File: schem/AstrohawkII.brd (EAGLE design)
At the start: 100 x 80 mm, 4 parts, among them J1 RASPBERRYPI-40-PIN-GPIO_PTH_N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

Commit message: updates eagle schematic and board
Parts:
- removed J3: (no value), SparkFun-Connectors:1X04
- removed J4: (no value), SparkFun-Connectors:1X06
- added U$1: BNO055, rocketry:BNO055
- moved J1 28.1 mm to (58.0, 10.0), turned to 180 degrees
- moved J2 16.7 mm to (41.4, 26.1)
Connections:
- removed net 3VO: J2.3, J4.2
- removed net ADR: J3.4
- removed net PS0: J3.1
- removed net PS1: J3.2
- net GND: no longer J4.3
- net INT: now also J1.29; no longer J3.3
- net INT1: now also J1.32
- net INT2: now also J1.33
- net RST: now also J1.31; no longer J4.6
- net SCL: no longer J4.5
- net SDA: no longer J4.4
- net VIN: no longer J4.1
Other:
- board size 100 x 80 mm -> 64 x 56 mm
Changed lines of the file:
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@@
 <setting verticaltext="up"/>
 </settings>
-<grid distance="50" unitdist="mil" unit="mil" style="lines" multiple="1" display="no" altdistance="5" altunitdist="mil" altunit="mil"/>
+<grid distance="1" unitdist="mm" unit="mm" style="lines" multiple="1" display="no" altdistance="0.5" altunitdist="mm" altunit="mm"/>
 <layers>
 <layer number="1" name="Top" color="4" fill="1" visible="yes" active="yes"/>
@@
 <board>
 <plain>
-<wire x1="0" y1="0" x2="100" y2="0" width="0" layer="20"/>
-<wire x1="100" y1="0" x2="100" y2="80" width="0" layer="20"/>
-<wire x1="100" y1="80" x2="0" y2="80" width="0" layer="20"/>
-<wire x1="0" y1="80" x2="0" y2="0" width="0" layer="20"/>
+<wire x1="0" y1="0" x2="64" y2="0" width="0" layer="20"/>
+<wire x1="64" y1="0" x2="64" y2="56" width="0" layer="20"/>
+<wire x1="64" y1="56" x2="0" y2="56" width="0" layer="20"/>
+<wire x1="0" y1="56" x2="0" y2="0" width="0" layer="20"/>
+<dimension x1="3" y1="53" x2="61" y2="53" x3="32" y3="53" textsize="1.778" layer="1"/>
 </plain>
 <attributes>
@@
 </autorouter>
 <elements>
-<element name="J1" library="SparkFun-Connectors" package="2X20" value="RASPBERRYPI-40-PIN-GPIO_PTH_NO_SHROUD" x="33.02" y="22.86" smashed="yes">
-<attribute name="NAME" x="31.75" y="26.924" size="0.6096" layer="25" font="vector" ratio="20"/>
-<attribute name="VALUE" x="31.75" y="20.447" size="0.6096" layer="27" font="vector" ratio="20"/>
+<element name="J1" library="SparkFun-Connectors" package="2X20" value="RASPBERRYPI-40-PIN-GPIO_PTH_NO_SHROUD" x="58" y="10" smashed="yes" rot="R180">
+<attribute name="NAME" x="59.27" y="5.936" size="0.6096" layer="25" font="vector" ratio="20" rot="R180"/>
+<attribute name="VALUE" x="59.27" y="12.413" size="0.6096" layer="27" font="vector" ratio="20" rot="R180"/>
 </element>
-<element name="J2" library="SparkFun-Connectors" package="1X07" value="" x="33.02" y="40.64" smashed="yes">
-<attribute name="MPL3115A2" value="" x="63.5" y="30.48" size="1.778" layer="27" display="off"/>
-<attribute name="NAME" x="31.75" y="42.037" size="0.6096" layer="25" font="vector" ratio="20"/>
-<attribute name="VALUE" x="31.75" y="38.608" size="0.6096" layer="27" font="vector" ratio="20"/>
+<element name="J2" library="SparkFun-Connectors" package="1X07" value="" x="41.42" y="26.15" smashed="yes">
+<attribute name="MPL3115A2" value="" x="71.9" y="15.99" size="1.778" layer="27" display="off"/>
+<attribute name="NAME" x="41.15" y="28.547" size="0.6096" layer="25" font="vector" ratio="20"/>
+<attribute name="VALUE" x="40.15" y="24.118" size="0.6096" layer="27" font="vector" ratio="20"/>
 </element>
-<element name="J3" library="SparkFun-Connectors" package="1X04" value="" x="60.96" y="52.07" smashed="yes">
-<attribute name="BNO055X04" value="" x="83.82" y="34.29" size="1.778" layer="27" display="off"/>
-<attribute name="NAME" x="59.69" y="53.467" size="0.6096" layer="25" font="vector" ratio="20"/>
-<attribute name="PROD_ID" value="CONN-09696" x="83.82" y="34.29" size="1.778" layer="27" display="off"/>
-<attribute name="VALUE" x="59.69" y="50.038" size="0.6096" layer="27" font="vector" ratio="20"/>
-</element>
-<element name="J4" library="SparkFun-Connectors" package="1X06" value="" x="45.72" y="59.69" smashed="yes">
-<attribute name="BNO055X06" value="" x="73.66" y="45.72" size="1.778" layer="27" display="off"/>
-<attribute name="NAME" x="44.45" y="61.087" size="0.6096" layer="25" font="vector" ratio="20"/>
-<attribute name="PROD_ID" value="CONN-08437" x="73.66" y="45.72" size="1.778" layer="27" display="off"/>
-<attribute name="VALUE" x="44.45" y="57.658" size="0.6096" layer="27" font="vector" ratio="20"/>
+<element name="U$1" library="rocketry" package="BNO055" value="BNO055" x="9.7" y="23.53" smashed="yes">
+<attribute name="NAME" x="12.24" y="36.23" size="1.778" layer="25"/>
+<attribute name="VALUE" x="12.24" y="29.88" size="1.778" layer="27"/>
 </element>
 </elements>
@@
 <contactref element="J1" pad="1"/>
 <contactref element="J1" pad="17"/>
-<wire x1="53.34" y1="22.86" x2="33.02" y2="22.86" width="0" layer="19" extent="1-1"/>
-</signal>
-<signal name="PS0">
-<contactref element="J3" pad="1"/>
-</signal>
-<signal name="PS1">
-<contactref element="J3" pad="2"/>
-</signal>
-<signal name="INT">
-<contactref element="J3" pad="3"/>
-</signal>
-<signal name="ADR">
-<contactref element="J3" pad="4"/>
+<wire x1="37.68" y1="10" x2="58" y2="10" width="0" layer="19" extent="1-1"/>
 </signal>
 <signal name="VIN">
 <contactref element="J2" pad="1"/>
-<contactref element="J4" pad="1"/>
 <contactref element="J1" pad="2"/>
 <contactref element="J1" pad="4"/>
-<wire x1="35.56" y1="25.4" x2="33.02" y2="25.4" width="0" layer="19" extent="1-1"/>
-<wire x1="33.02" y1="40.64" x2="35.56" y2="25.4" width="0" layer="19" extent="1-1"/>
-<wire x1="45.72" y1="59.69" x2="33.02" y2="40.64" width="0" layer="19" extent="1-1"/>
+<wire x1="58" y1="7.46" x2="41.42" y2="26.15" width="0" layer="19" extent="1-1"/>
+<wire x1="55.46" y1="7.46" x2="58" y2="7.46" width="0" layer="19" extent="1-1"/>
 </signal>
 <signal name="GND">
 <contactref element="J2" pad="2"/>
-<contactref element="J4" pad="3"/>
 <contactref element="J1" pad="6"/>
 <contactref element="J1" pad="9"/>
@@
 <contactref element="J1" pad="34"/>
 <contactref element="J1" pad="39"/>
-<wire x1="43.18" y1="22.86" x2="38.1" y2="25.4" width="0" layer="19" extent="1-1"/>
-<wire x1="48.26" y1="25.4" x2="43.18" y2="22.86" width="0" layer="19" extent="1-1"/>
-<wire x1="55.88" y1="25.4" x2="48.26" y2="25.4" width="0" layer="19" extent="1-1"/>
-<wire x1="63.5" y1="22.86" x2="55.88" y2="25.4" width="0" layer="19" extent="1-1"/>
-<wire x1="68.58" y1="25.4" x2="63.5" y2="22.86" width="0" layer="19" extent="1-1"/>
-<wire x1="35.56" y1="40.64" x2="68.58" y2="25.4" width="0" layer="19" extent="1-1"/>
-<wire x1="73.66" y1="25.4" x2="68.58" y2="25.4" width="0" layer="19" extent="1-1"/>
-<wire x1="50.8" y1="59.69" x2="35.56" y2="40.64" width="0" layer="19" extent="1-1"/>
-<wire x1="81.28" y1="22.86" x2="73.66" y2="25.4" width="0" layer="19" extent="1-1"/>
-</signal>
-<signal name="3VO">
-<contactref element="J2" pad="3"/>
-<contactref element="J4" pad="2"/>
-<wire x1="48.26" y1="59.69" x2="38.1" y2="40.64" width="0" layer="19" extent="1-1"/>
+<wire x1="17.36" y1="7.46" x2="9.74" y2="10" width="0" layer="19" extent="1-1"/>
+<wire x1="22.44" y1="7.46" x2="17.36" y2="7.46" width="0" layer="19" extent="1-1"/>
+<wire x1="27.52" y1="10" x2="22.44" y2="7.46" width="0" layer="19" extent="1-1"/>
+<wire x1="35.14" y1="7.46" x2="27.52" y2="10" width="0" layer="19" extent="1-1"/>
+<wire x1="42.76" y1="7.46" x2="35.14" y2="7.46" width="0" layer="19" extent="1-1"/>
+<wire x1="47.84" y1="10" x2="42.76" y2="7.46" width="0" layer="19" extent="1-1"/>
+<wire x1="52.92" y1="7.46" x2="47.84" y2="10" width="0" layer="19" extent="1-1"/>
+<wire x1="43.96" y1="26.15" x2="52.92" y2="7.46" width="0" layer="19" extent="1-1"/>
 </signal>
 <signal name="INT2">
 <contactref element="J2" pad="4"/>
+<contactref element="J1" pad="33"/>
+<wire x1="49.04" y1="26.15" x2="17.36" y2="10" width="0" layer="19" extent="1-1"/>
 </signal>
 <signal name="INT1">
 <contactref element="J2" pad="5"/>
+<contactref element="J1" pad="32"/>
+<wire x1="51.58" y1="26.15" x2="19.9" y2="7.46" width="0" layer="19" extent="1-1"/>
 </signal>
 <signal name="SCL">
 <contactref element="J2" pad="6"/>
-<contactref element="J4" pad="5"/>
 <contactref element="J1" pad="5"/>
-<wire x1="45.72" y1="40.64" x2="38.1" y2="22.86" width="0" layer="19" extent="1-1"/>
-<wire x1="55.88" y1="59.69" x2="45.72" y2="40.64" width="0" layer="19" extent="1-1"/>
+<wire x1="52.92" y1="10" x2="54.12" y2="26.15" width="0" layer="19" extent="1-1"/>
 </signal>
 <signal name="SDA">
 <contactref element="J2" pad="7"/>
-<contactref element="J4" pad="4"/>
 <contactref element="J1" pad="3"/>
-<wire x1="53.34" y1="59.69" x2="35.56" y2="22.86" width="0" layer="19" extent="1-1"/>
-<wire x1="48.26" y1="40.64" x2="53.34" y2="59.69" width="0" layer="19" extent="1-1"/>
+<wire x1="55.46" y1="10" x2="56.66" y2="26.15" width="0" layer="19" extent="1-1"/>
+</signal>
+<signal name="INT">
+<contactref element="J1" pad="29"/>
 </signal>
 <signal name="RST">
-<contactref element="J4" pad="6"/>
+<contactref element="J1" pad="31"/>
+</signal>
+<signal name="N$1">
+<via x="3.5" y="52.5" extent="1-16" drill="2.75" diameter="6"/>
+</signal>
+<signal name="N$2">
+<via x="3.5" y="3.5" extent="1-16" drill="2.75" diameter="6"/>
+</signal>
+<signal name="N$3">
+<via x="60.5" y="3.5" extent="1-16" drill="2.75" diameter="6"/>
+</signal>
+<signal name="N$4">
+<via x="60.5" y="52.5" extent="1-16" drill="2.75" diameter="6"/>
 </signal>
 </signals>

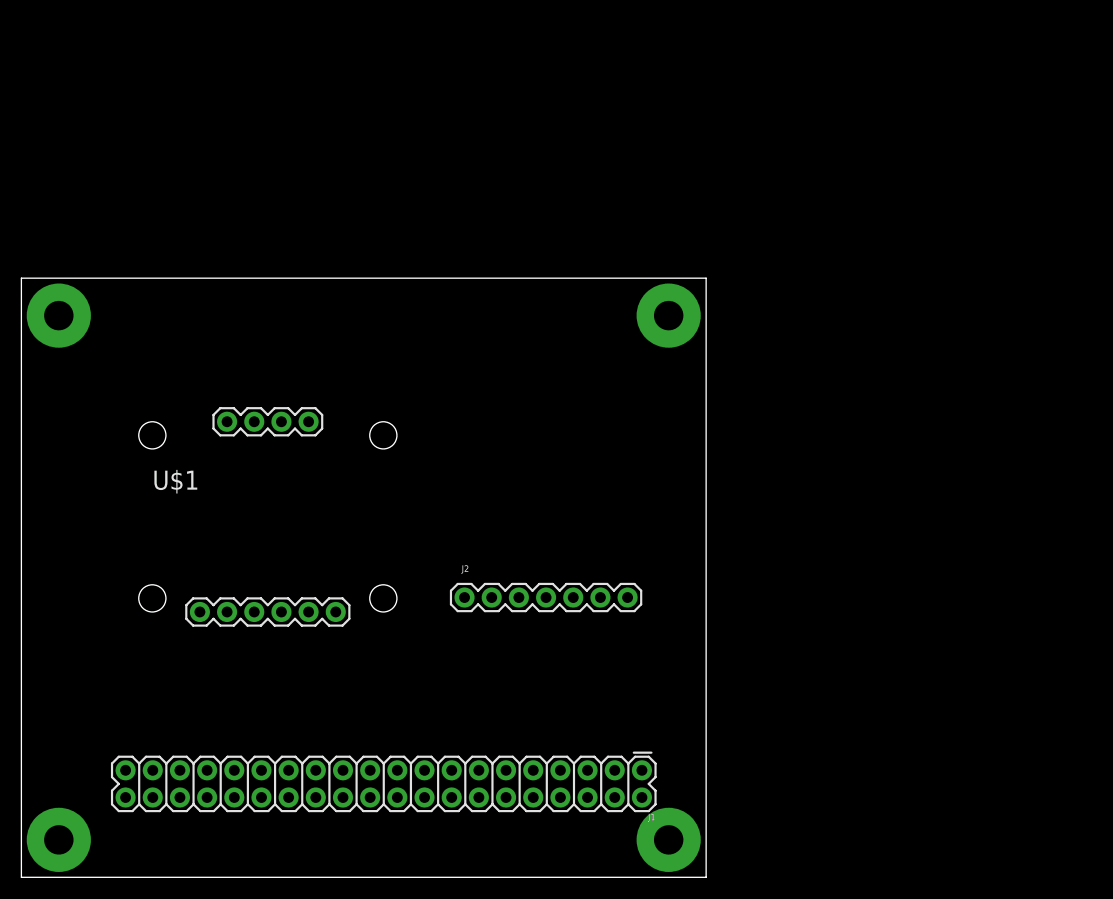
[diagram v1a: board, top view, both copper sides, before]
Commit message: fixes holes for raspberry pi
This change fixes the holes for the raspberry pi, adds
measurement lines showing the correct dimensions, and
updates the IMU part because the pins were backwards on
the symbol.
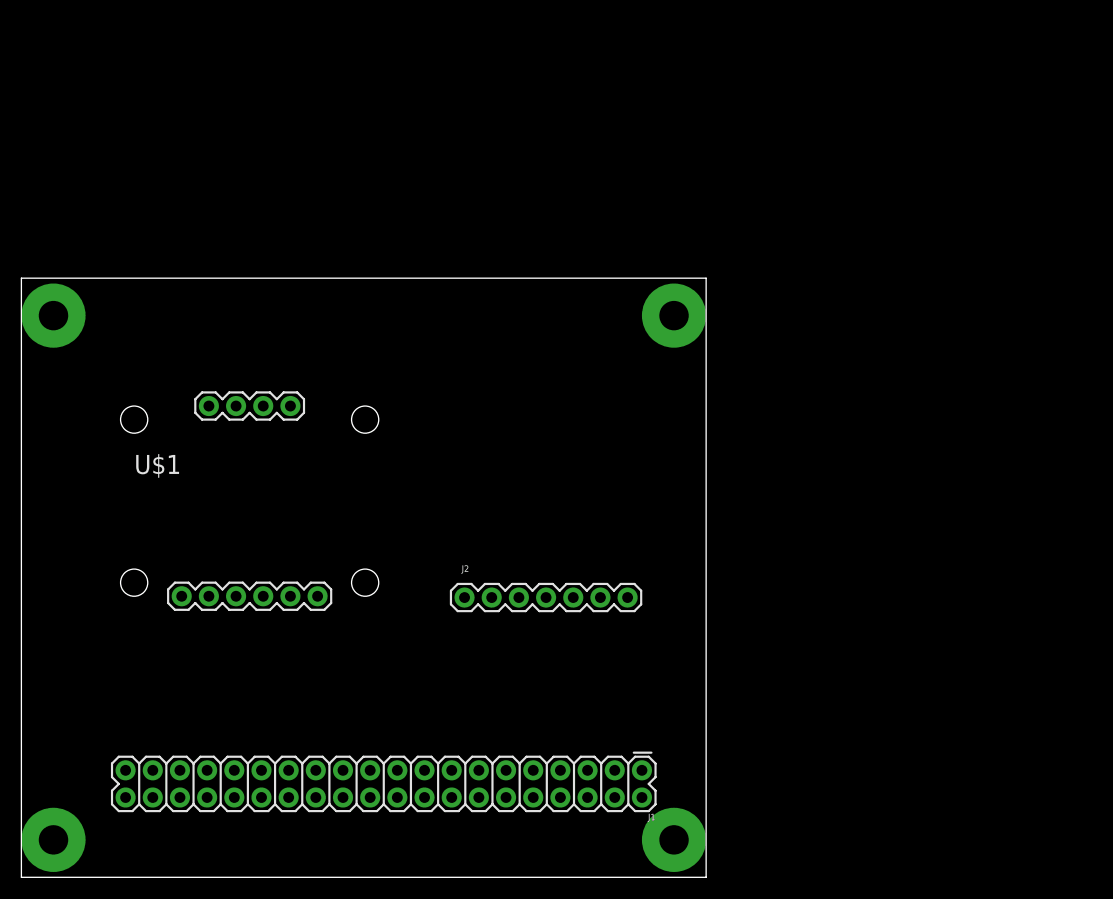
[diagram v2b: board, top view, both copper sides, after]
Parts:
- moved U$1 2.25 mm to (8.00, 25.0)
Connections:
- new net ADR: U$1.ADR
- new net PS0: U$1.PS0
- new net PS1: U$1.PS1
- net GND: now also U$1.GND
- net INT: now also U$1.INT
- net RST: now also U$1.RST
- net SCL: now also U$1.SCL
- net SDA: now also U$1.SDA
- net VIN: now also U$1.VIN
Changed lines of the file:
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@@
 <?xml version="1.0" encoding="utf-8"?>
 <!DOCTYPE eagle SYSTEM "eagle.dtd">
-<eagle version="9.5.2">
+<eagle version="8.2.2">
 <drawing>
 <settings>
@@
 <wire x1="64" y1="56" x2="0" y2="56" width="0" layer="20"/>
 <wire x1="0" y1="56" x2="0" y2="0" width="0" layer="20"/>
-<dimension x1="3" y1="53" x2="61" y2="53" x3="32" y3="53" textsize="1.778" layer="1"/>
+<dimension x1="3" y1="52" x2="61" y2="52" x3="32" y3="66" textsize="1.778" layer="51"/>
+<dimension x1="3" y1="3.5" x2="3" y2="52.5" x3="-12" y3="28" textsize="1.778" layer="51"/>
 </plain>
 <attributes>
@@
 <param name="dpMaxLengthDifference" value="10mm"/>
 <param name="dpGapFactor" value="2.5"/>
+<param name="checkGrid" value="0"/>
 <param name="checkAngle" value="0"/>
 <param name="checkFont" value="1"/>
 <param name="checkRestrict" value="1"/>
-<param name="checkStop" value="0"/>
-<param name="checkValues" value="0"/>
-<param name="checkNames" value="1"/>
-<param name="checkWireStubs" value="1"/>
-<param name="checkPolygonWidth" value="0"/>
 <param name="useDiameter" value="13"/>
 <param name="maxErrors" value="50"/>
@@
 <attribute name="VALUE" x="40.15" y="24.118" size="0.6096" layer="27" font="vector" ratio="20"/>
 </element>
-<element name="U$1" library="rocketry" package="BNO055" value="BNO055" x="9.7" y="23.53" smashed="yes">
-<attribute name="NAME" x="12.24" y="36.23" size="1.778" layer="25"/>
-<attribute name="VALUE" x="12.24" y="29.88" size="1.778" layer="27"/>
-</element>
+<element name="U$1" library="rocketry" package="BNO055" value="BNO055" x="8" y="25"/>
 </elements>
 <signals>
@@
 <contactref element="J1" pad="2"/>
 <contactref element="J1" pad="4"/>
-<wire x1="58" y1="7.46" x2="41.42" y2="26.15" width="0" layer="19" extent="1-1"/>
-<wire x1="55.46" y1="7.46" x2="58" y2="7.46" width="0" layer="19" extent="1-1"/>
+<contactref element="U$1" pad="VIN"/>
+<wire x1="55.46" y1="7.46" x2="41.42" y2="26.15" width="0" layer="19" extent="1-1"/>
+<wire x1="58" y1="7.46" x2="55.46" y2="7.46" width="0" layer="19" extent="1-1"/>
+<wire x1="14.985" y1="26.27" x2="41.42" y2="26.15" width="0" layer="19" extent="1-1"/>
 </signal>
 <signal name="GND">
@@
 <contactref element="J1" pad="34"/>
 <contactref element="J1" pad="39"/>
-<wire x1="17.36" y1="7.46" x2="9.74" y2="10" width="0" layer="19" extent="1-1"/>
-<wire x1="22.44" y1="7.46" x2="17.36" y2="7.46" width="0" layer="19" extent="1-1"/>
-<wire x1="27.52" y1="10" x2="22.44" y2="7.46" width="0" layer="19" extent="1-1"/>
-<wire x1="35.14" y1="7.46" x2="27.52" y2="10" width="0" layer="19" extent="1-1"/>
-<wire x1="42.76" y1="7.46" x2="35.14" y2="7.46" width="0" layer="19" extent="1-1"/>
-<wire x1="47.84" y1="10" x2="42.76" y2="7.46" width="0" layer="19" extent="1-1"/>
+<contactref element="U$1" pad="GND"/>
+<wire x1="47.84" y1="10" x2="43.96" y2="26.15" width="0" layer="19" extent="1-1"/>
 <wire x1="52.92" y1="7.46" x2="47.84" y2="10" width="0" layer="19" extent="1-1"/>
-<wire x1="43.96" y1="26.15" x2="52.92" y2="7.46" width="0" layer="19" extent="1-1"/>
+<wire x1="42.76" y1="7.46" x2="47.84" y2="10" width="0" layer="19" extent="1-1"/>
+<wire x1="35.14" y1="7.46" x2="42.76" y2="7.46" width="0" layer="19" extent="1-1"/>
+<wire x1="27.52" y1="10" x2="35.14" y2="7.46" width="0" layer="19" extent="1-1"/>
+<wire x1="22.44" y1="7.46" x2="27.52" y2="10" width="0" layer="19" extent="1-1"/>
+<wire x1="17.36" y1="7.46" x2="22.44" y2="7.46" width="0" layer="19" extent="1-1"/>
+<wire x1="9.74" y1="10" x2="17.36" y2="7.46" width="0" layer="19" extent="1-1"/>
+<wire x1="20.065" y1="26.27" x2="9.74" y2="10" width="0" layer="19" extent="1-1"/>
 </signal>
 <signal name="INT2">
@@
 <contactref element="J2" pad="6"/>
 <contactref element="J1" pad="5"/>
+<contactref element="U$1" pad="SCL"/>
 <wire x1="52.92" y1="10" x2="54.12" y2="26.15" width="0" layer="19" extent="1-1"/>
+<wire x1="25.145" y1="26.27" x2="52.92" y2="10" width="0" layer="19" extent="1-1"/>
 </signal>
 <signal name="SDA">
 <contactref element="J2" pad="7"/>
 <contactref element="J1" pad="3"/>
+<contactref element="U$1" pad="SDA"/>
 <wire x1="55.46" y1="10" x2="56.66" y2="26.15" width="0" layer="19" extent="1-1"/>
+<wire x1="22.605" y1="26.27" x2="55.46" y2="10" width="0" layer="19" extent="1-1"/>
 </signal>
 <signal name="INT">
 <contactref element="J1" pad="29"/>
+<contactref element="U$1" pad="INT"/>
+<wire x1="22.605" y1="44.05" x2="22.44" y2="10" width="0" layer="19" extent="1-1"/>
 </signal>
 <signal name="RST">
 <contactref element="J1" pad="31"/>
+<contactref element="U$1" pad="RST"/>
+<wire x1="27.685" y1="26.27" x2="19.9" y2="10" width="0" layer="19" extent="1-1"/>
 </signal>
 <signal name="N$1">
-<via x="3.5" y="52.5" extent="1-16" drill="2.75" diameter="6"/>
+<via x="3" y="52.5" extent="1-16" drill="2.75" diameter="6"/>
 </signal>
 <signal name="N$2">
-<via x="3.5" y="3.5" extent="1-16" drill="2.75" diameter="6"/>
+<via x="3" y="3.5" extent="1-16" drill="2.75" diameter="6"/>
 </signal>
 <signal name="N$3">
-<via x="60.5" y="3.5" extent="1-16" drill="2.75" diameter="6"/>
+<via x="61" y="3.5" extent="1-16" drill="2.75" diameter="6"/>
 </signal>
 <signal name="N$4">
-<via x="60.5" y="52.5" extent="1-16" drill="2.75" diameter="6"/>
+<via x="61" y="52.5" extent="1-16" drill="2.75" diameter="6"/>
+</signal>
+<signal name="PS0">
+<contactref element="U$1" pad="PS0"/>
+</signal>
+<signal name="PS1">
+<contactref element="U$1" pad="PS1"/>
+</signal>
+<signal name="ADR">
+<contactref element="U$1" pad="ADR"/>
 </signal>
 </signals>
-<mfgpreviewcolors>
-<mfgpreviewcolor name="soldermaskcolor" color="0xC8008000"/>
-<mfgpreviewcolor name="silkscreencolor" color="0xFFFEFEFE"/>
-<mfgpreviewcolor name="backgroundcolor" color="0xFF282828"/>
-<mfgpreviewcolor name="coppercolor" color="0xFFFFBF00"/>
-<mfgpreviewcolor name="substratecolor" color="0xFF786E46"/>
-</mfgpreviewcolors>
 </board>
 </drawing>
